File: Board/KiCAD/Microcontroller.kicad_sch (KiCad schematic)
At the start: 29 parts, among them J2 Conn_ARM_SWD_TagConnect_TC2030, J4 Conn_01x03, SW2 SW_Push, U5 LMR50410, U9 STM32F103C8T6, Y1 Crystal_GND24_Small, Y4 CM8V-T1A-32.768KHZ-12.5PF-20P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

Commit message: PCB Optimization
Made changes to the PCB to make it smaller, as well as adding the Castellated Vias

@andrewgreenberg
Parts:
- J2: footprint Connector:Tag-Connect_TC2030-IDC-FP_2x03_P1.27mm_Vertical -> Connector:Tag-Connect_TC2030-IDC-NL_2x03_P1.27mm_Vertical
- TP39: footprint TestPoint:TestPoint_THTPad_1.0x1.0mm_Drill0.5mm -> TestPoint:TestPoint_Pad_1.0x1.0mm
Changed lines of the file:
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@@
 			)
 		)
-		(property "Footprint" "TestPoint:TestPoint_THTPad_1.0x1.0mm_Drill0.5mm"
+		(property "Footprint" "TestPoint:TestPoint_Pad_1.0x1.0mm"
 			(at 81.28 44.45 0)
 			(effects
@@
 			)
 		)
-		(property "Footprint" "Connector:Tag-Connect_TC2030-IDC-FP_2x03_P1.27mm_Vertical"
+		(property "Footprint" "Connector:Tag-Connect_TC2030-IDC-NL_2x03_P1.27mm_Vertical"
 			(at 165.1 62.23 0)
 			(effects

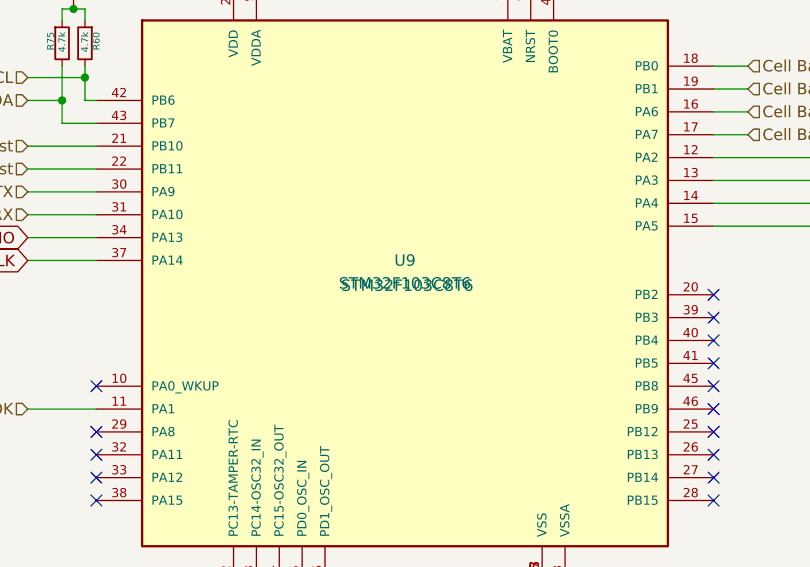
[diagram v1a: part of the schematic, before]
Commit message: Cleaned up BOM materials again. Why do these keep reseting? Also, big refactor on cell balancing circuits and battery connection (NOW FLIPPED) to make board smaller. More smallification is left as an exercise to the reader.
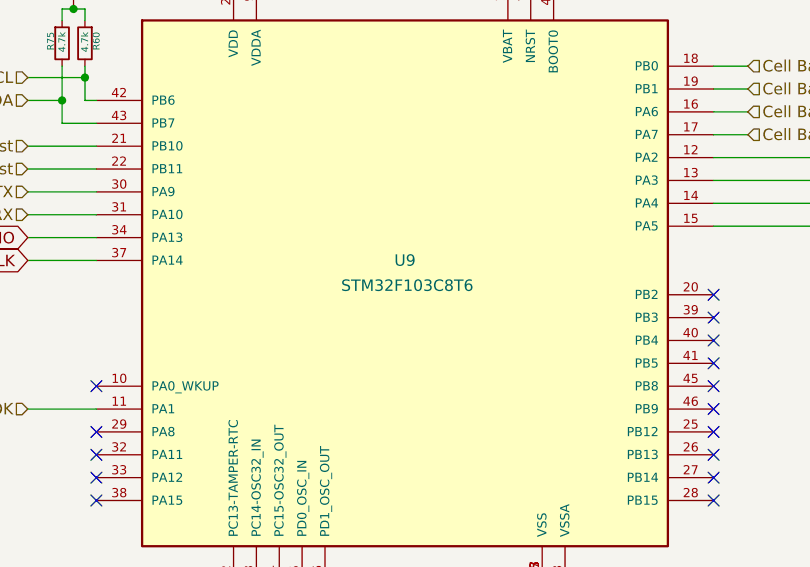
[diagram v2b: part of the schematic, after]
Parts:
- C30, C31, C32, C33: Package 600S200FT250XT4K -> (none)
- C34, C54, C55, C56, C57, C58: Package CL05B104KA5NNNC -> (none)
- C51: Package TMK107ABJ225KA-T -> (none)
- C52, C53: Package CL31B106KAHNNNE -> (none)
- J2: Package TC2030-CTX -> (none)
- J4: Package 61300311121 -> (none)
- L3: Package MAMK2520T3R3M -> (none)
- R58: Package MCF0603FT100K -> (none)
- R60, R75: Package RMCF0603FT4K70 -> (none)
- R61, R73, R77, R78: Package RMCF0603FT10K0 -> (none)
- SW2: Package PTS526SM15SMTR2 LFS -> (none)
- U5: Package LMR50410XFDBVR -> (none)
- U9: Package STM32F103C8T6 -> (none)
- Y1: Package 7V-8.000MDDQ-T -> (none)
- Y4: Package CM8V-T1A-32.768KHZ-12.5PF-20PPM-TA-QA -> (none)

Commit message: EPL - Battery Management System REV 2
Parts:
- added D1, D2, D3, D4: LED_Small, LED_SMD:LED_0603_1608Metric, symbol Device:LED_Small
- added R74, R79, R80, R81: 1k, Resistor_SMD:R_0603_1608Metric, symbol Device:R_Small
- SW2: footprint Button_Switch_SMD:SW_Push_1P1T_NO_CK_KMR2 -> Button_Switch_SMD:SW_Push_SPST_NO_Alps_SKRK
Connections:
- net GND: now also D1.1 (K), D2.1 (K), D3.1 (K), D4.1 (K)
- net at U9.25 (PB12): now also R74.2
- net at U9.26 (PB13): now also R79.1
- net at U9.27 (PB14): now also R80.1
- net at U9.28 (PB15): now also R81.1
- new net: D3.2 (A), R79.2
- new net: D2.2 (A), R80.2
- new net: D4.2 (A), R74.1
- new net: D1.2 (A), R81.2
- no-connect marks 16 -> 12
